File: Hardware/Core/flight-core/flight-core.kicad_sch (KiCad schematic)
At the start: 44 parts, among them J10 Conn_02x05_Counter_Clockwise, J101 Conn_01x02, J12 Conn_02x05_Counter_Clockwise, J2 Conn_01x08, J20 Conn_01x04, J21 Conn_01x02, J22 Conn_01x02, J23 Conn_01x02, J24 Conn_01x02, J25 Conn_01x02, J26 Conn_01x02, J27 Conn_01x02, J28 Conn_01x02, J29 Conn_01x02, J3 Conn_01x02, J30 Conn_01x02, J4 Conn_01x02, J5 Cube Orange Plus Female Header, J6 Conn_01x02, J7 Conn_01x02, J8 Conn_02x05_Counter_Clockwise, J9 Conn_02x05_Counter_Clockwise, U10 LTV-356T, U103 LTV-356T, U11 LTV-356T, U12 18-75V to 5V Converter, U2 LTV-356T, U3 LTV-356T, U4 TPS62086RLTR, U65 LTV-356T

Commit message: added reorganized main schematic and created draft of test_points_leds in stm32
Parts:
- removed C13: 10uF, footprints:C_0603_1608Metric, symbol Device:C
- removed C2: 22uF, footprints:C_0603_1608Metric, symbol Device:C
- removed D1: LED_0805_Amber, footprints:LED_0805_OEM, symbol formula:LED_0805_Amber
- removed J101, J21, J22, J23, J24, J25, J26, J27, J28, J29, J3, J4, J6, J7: Conn_01x02, symbol Connector_Generic:Conn_01x02
- removed J5: Cube Orange Plus Female Header, DF17_4.0_-80DP-0.5V_57_:HRS_DF17_4.0_-80DP-0.5V_57_, symbol formula:DF17_4.0_-80DP-0.5V_57_
- removed L1: 470nH, obad_footprints:IND_XFL4015_COC, symbol OlinBAD:XFL4015-471MEC
- removed R2, R4: 120, OEM:R_0603, symbol OEM:120R
- removed R3: 100K, footprints:R_0805_OEM, symbol formula:R_100K
- removed R5: 1M, footprints:R_0603_1608Metric, symbol Device:R
- removed R6, R7: 330, OEM:R_0603_1608Metric, symbol OEM:1KR
- removed U10, U65: LTV-356T, Package_SO:SO-4_4.4x3.6mm_P2.54mm, symbol Isolator:LTV-356T
- removed U12: 18-75V to 5V Converter, obad_footprints:UWE-Q12_MUR, symbol OlinBAD:E36SC05025NRFA
- removed U4: TPS62086RLTR, obad_footprints:RLT0007A, symbol OlinBAD:TPS62086RLTR
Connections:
- net SHDN_SENSE_STM is gone; now on net SHDN_CRITICAL: J30.1 (Pin_1)
- net ARM renamed SHDN_CRITICAL
- no-connect marks 1 -> 0
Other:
- added sheet Cube 1 Header (cube_1.kicad_sch)
- added sheet Power Supplies (converters.kicad_sch)
- added sheet Shutdown Nodes (shdn.kicad_sch)
- sheet stm32 ports: added BMS_EN, CTRL_SANITY_CHECK, SHDN_SENSE_ALL_BATT, SHDN_SENSE_BMS_MATE_E, SHDN_SENSE_BMS_MATE_N, SHDN_SENSE_BMS_MATE_S, SHDN_SENSE_BMS_MATE_W, SHDN_SENSE_BMS_OK_E, SHDN_SENSE_BMS_OK_N, SHDN_SENSE_BMS_OK_S, SHDN_SENSE_CUBE, SHDN_SENSE_E_ARM, SHDN_SENSE_FRAME_ESTOP, SHDN_SENSE_NE_ARM, SHDN_SENSE_NUC, SHDN_SENSE_NW_ARM, SHDN_SENSE_N_ARM, SHDN_SENSE_REMOTE_ESTOP, SHDN_SENSE_RIDER_ESTOP, SHDN_SENSE_SANITY, SHDN_SENSE_SE_ARM, SHDN_SENSE_SW_ARM, SHDN_SENSE_S_ARM, SHDN_SENSE_TILT, SHDN_SENSE_TSMS, SHDN_SENSE_WIRED_ESTOP, SHDN_SENSE_W_ARM; removed none
- note added: "Things left to do: - What current am i sensing? - which current sensor model should i use? schematic validation of that - LEDs & Test points - clean up the import of the led schematic on the stm page - Cube pinout - tilt shutdown? - antenna integration? - does it make sense to put shdn_critical in the output of each bms connector? - i forgot what BMS_EN was again - validate the schematic design o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"
- moved on the sheet: J10, J12, J2, J20, J30, J8, J9, R10, R107, R11, R12, U103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

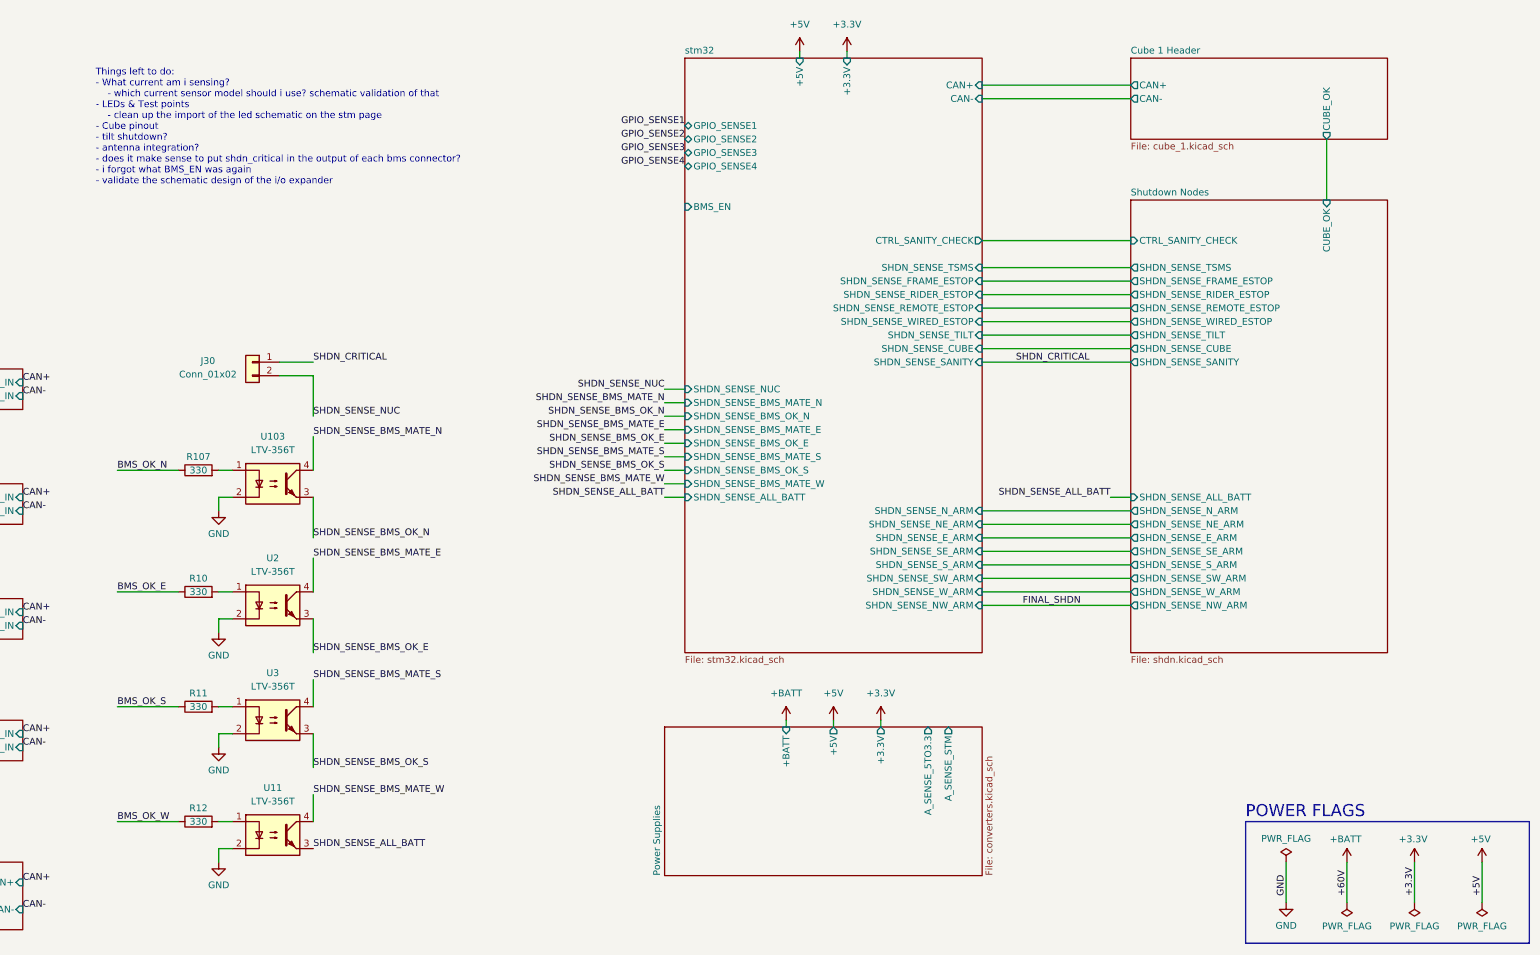
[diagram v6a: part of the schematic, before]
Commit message: added common mode filter on CAN term resistor; renamed cube_ok
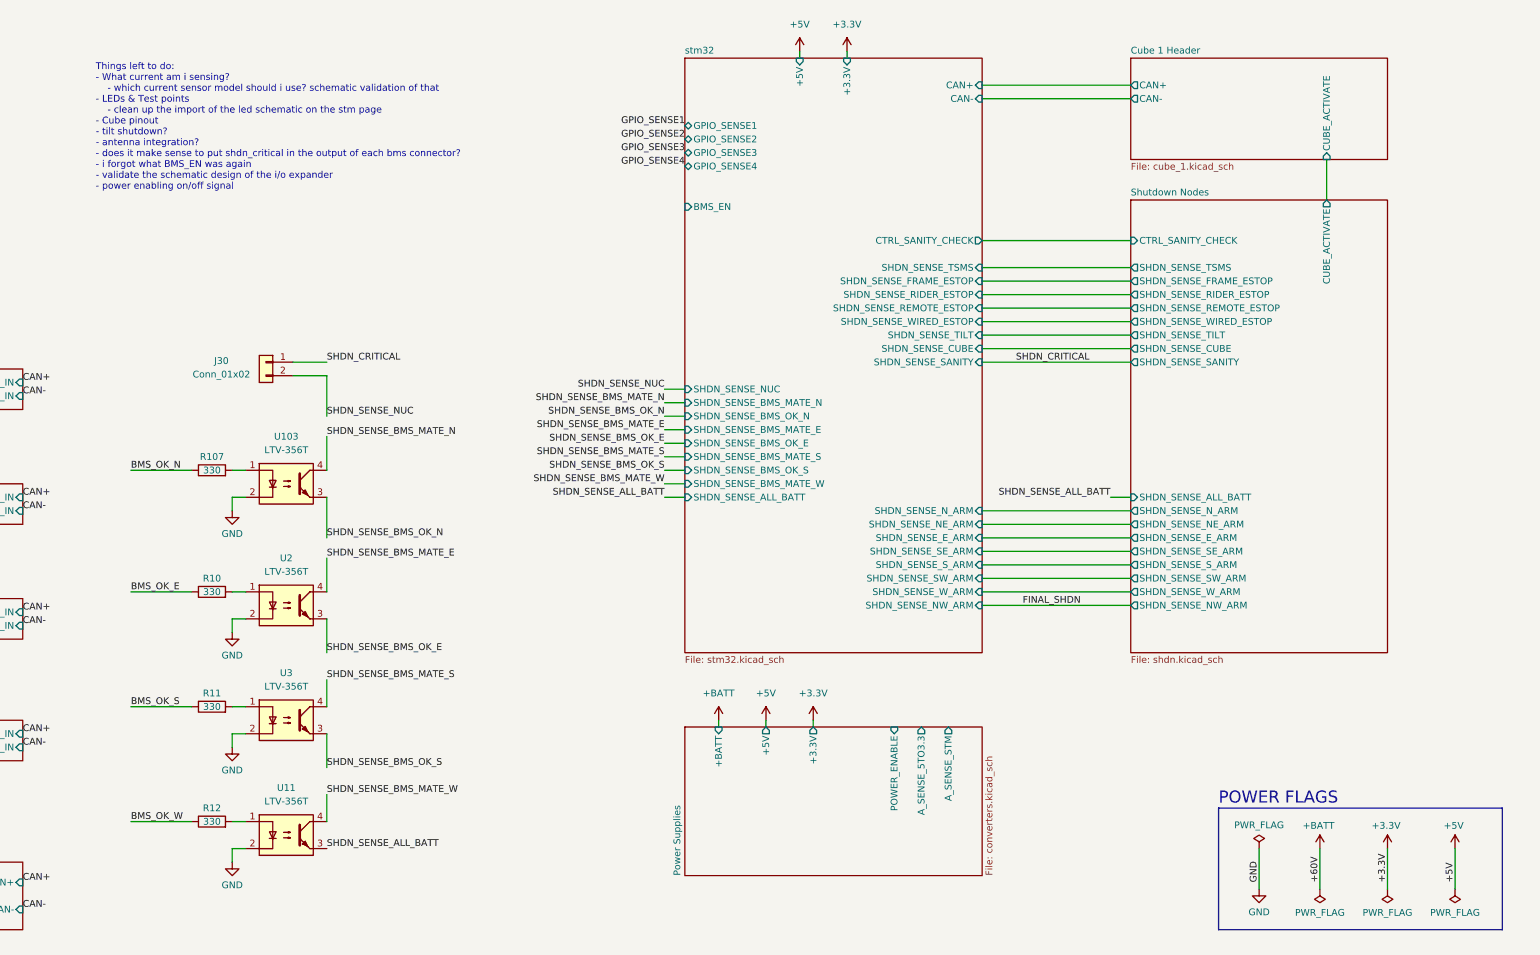
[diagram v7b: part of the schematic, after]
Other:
- sheet Cube 1 Header ports: added CUBE_ACTIVATE; removed CUBE_OK
- sheet Power Supplies ports: added POWER_ENABLE; removed none
- sheet Shutdown Nodes ports: added CUBE_ACTIVATE; removed CUBE_OK
- moved on the sheet: J30, R10, R107, R11, R12, U103, U11, U2, U3

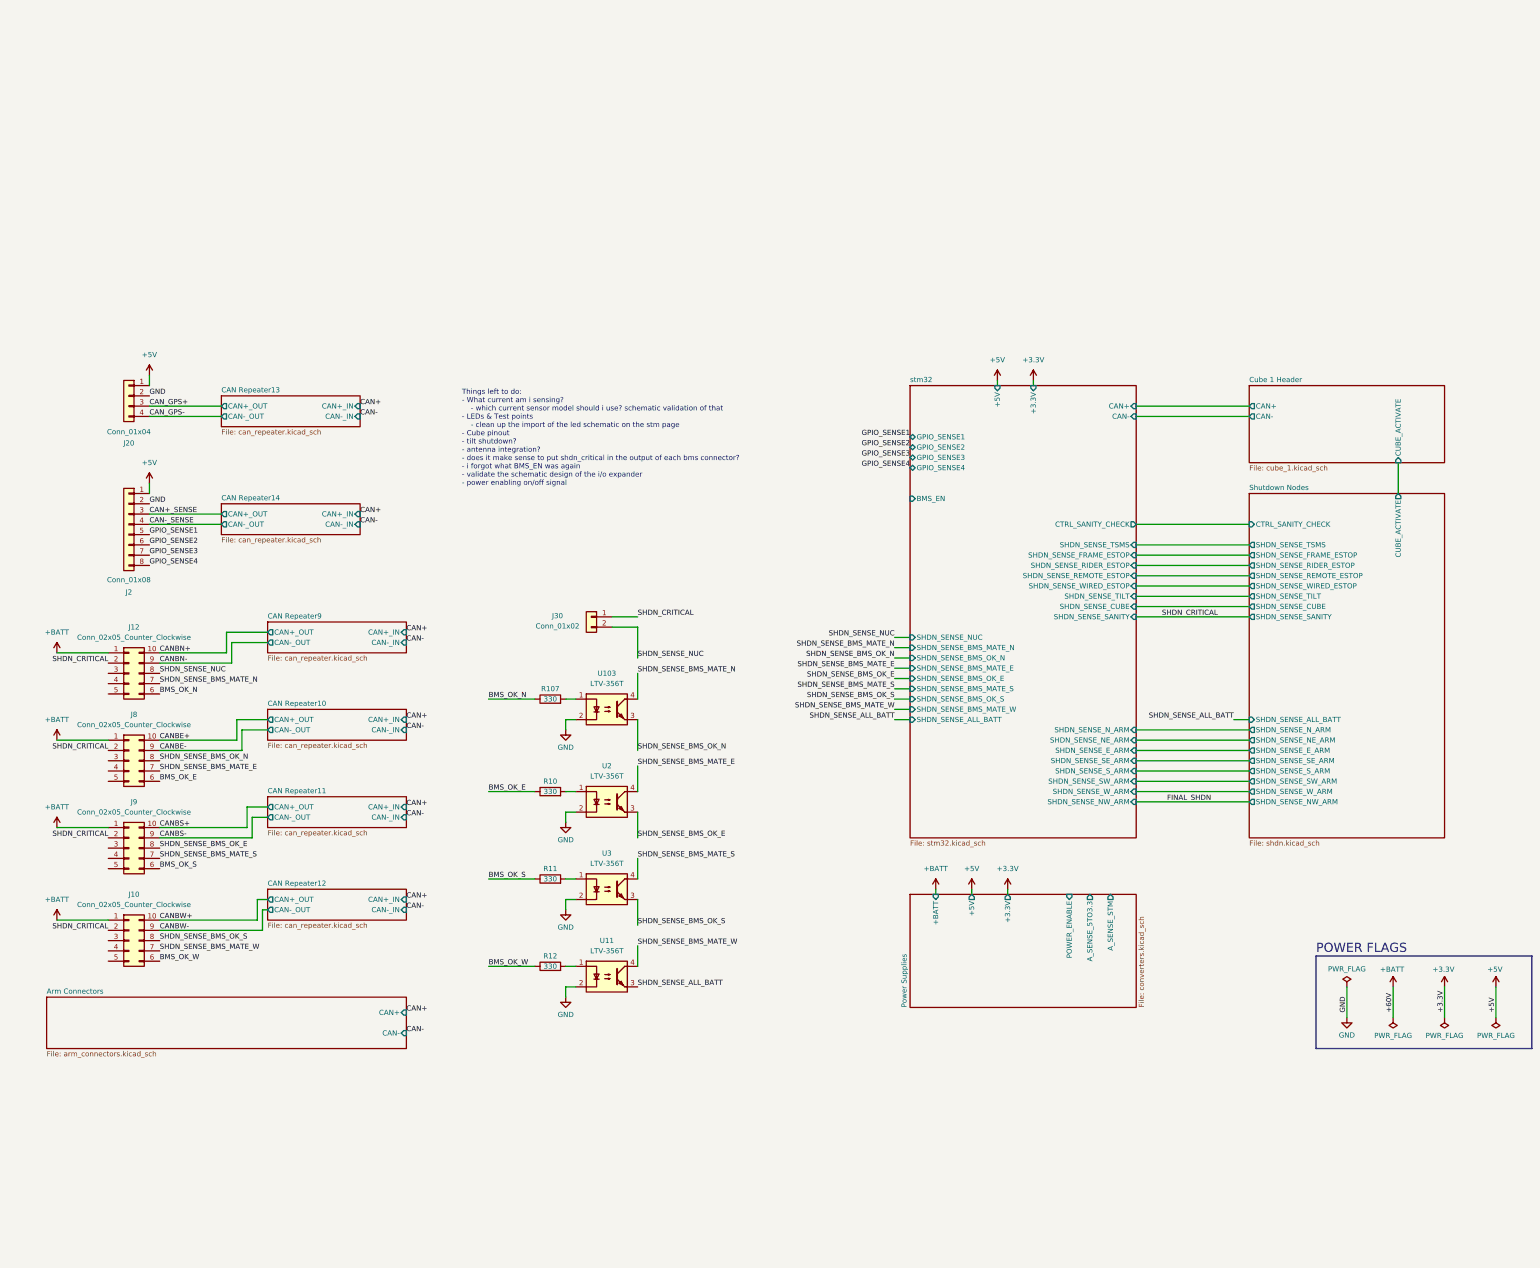
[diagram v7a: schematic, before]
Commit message: removed old MATE shdn nodes, added BMS_EN, reorganized and shrunk sheet size
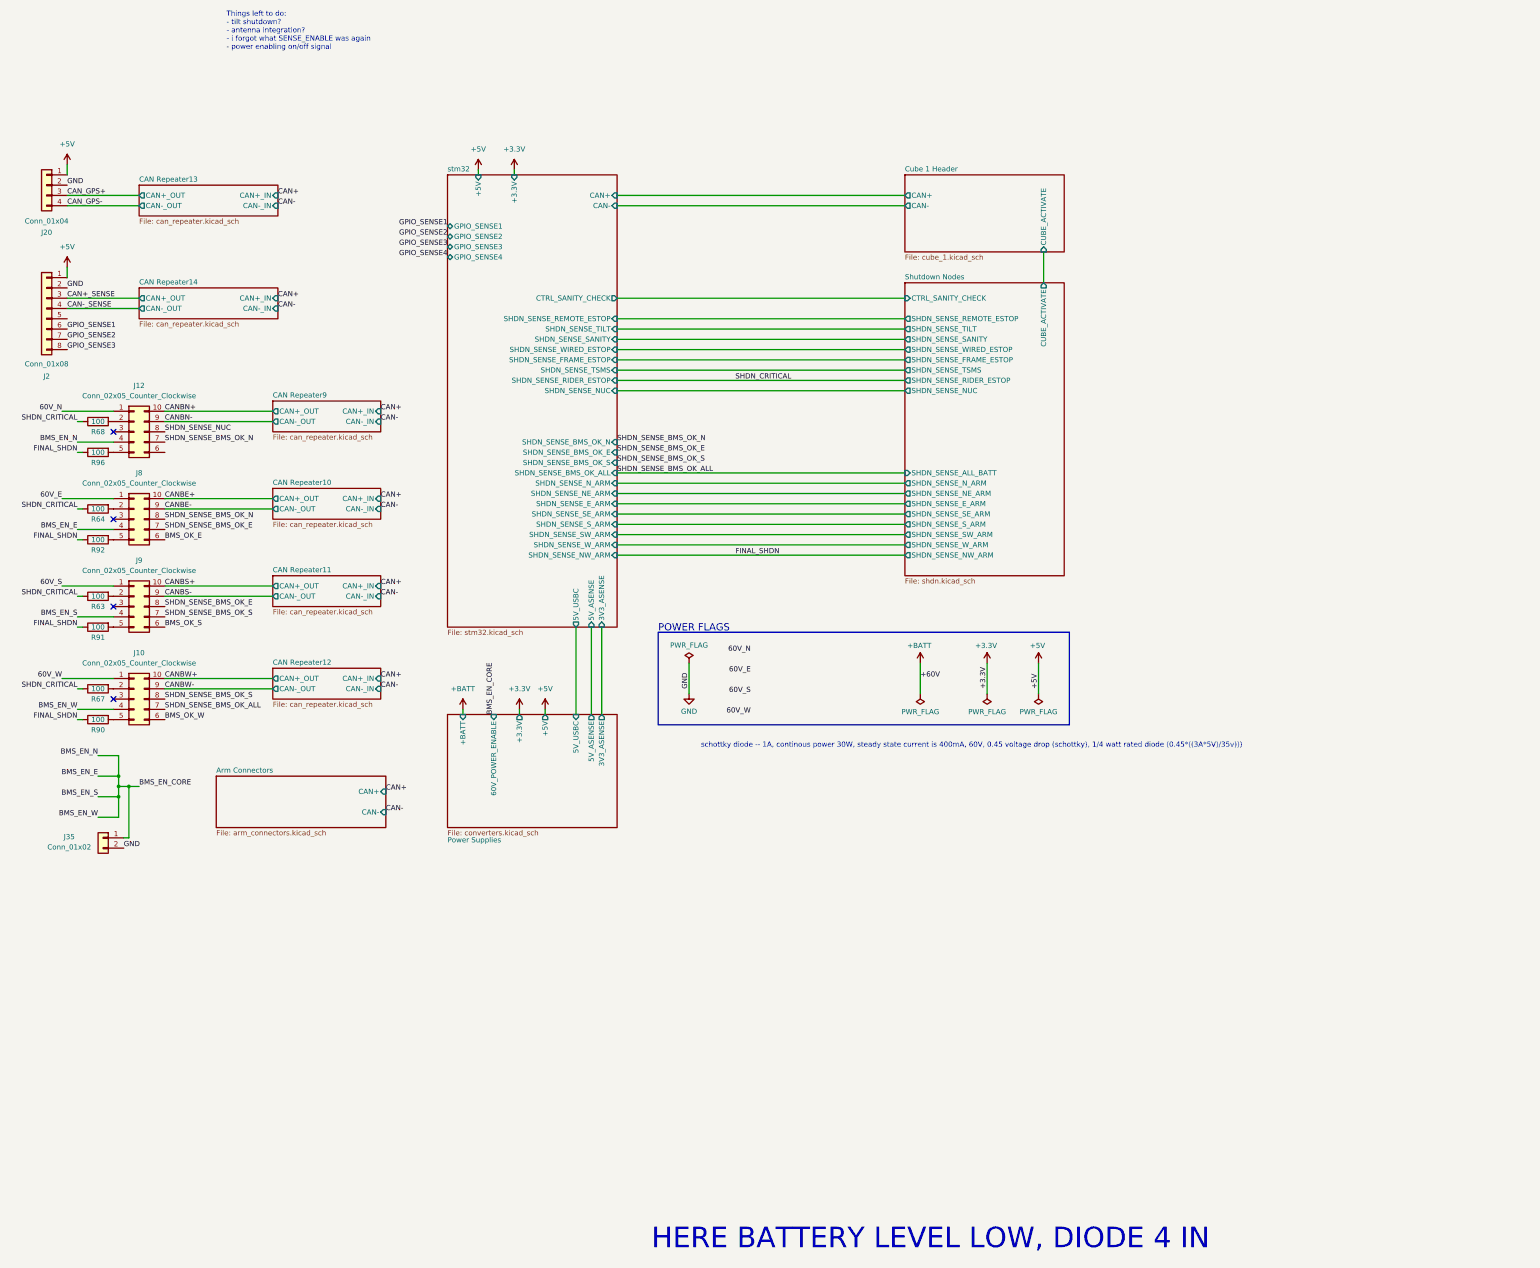
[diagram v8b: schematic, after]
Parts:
- removed J30: Conn_01x02, symbol Connector_Generic:Conn_01x02
- removed R10, R107, R11, R12: 330, OEM:R_0603_1608Metric, symbol OEM:1KR
- removed U103, U11, U2, U3: LTV-356T, Package_SO:SO-4_4.4x3.6mm_P2.54mm, symbol Isolator:LTV-356T
- added J35: Conn_01x02, symbol Connector_Generic:Conn_01x02
- added R63, R64, R67, R68, R90, R91, R92, R96: 100, footprints:R_0603_1608Metric, symbol Device:R
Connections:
- net SHDN_SENSE_BMS_MATE_E is gone; now on net SHDN_SENSE_BMS_OK_E: J8.7 (Pin_7)
- net SHDN_SENSE_BMS_MATE_N is gone; now on net SHDN_SENSE_BMS_OK_N: J12.7 (Pin_7)
- net SHDN_SENSE_BMS_MATE_S is gone; now on net SHDN_SENSE_BMS_OK_S: J9.7 (Pin_7)
- net +BATT: no longer J10.1 (Pin_1), J12.1 (Pin_1), J8.1 (Pin_1), J9.1 (Pin_1)
- net FINAL_SHDN: now also R90.1, R91.1, R92.1, R96.1
- net GND: now also J35.2 (Pin_2)
- net GPIO_SENSE1: now also J2.6 (Pin_6); no longer J2.5 (Pin_5)
- net GPIO_SENSE2: now also J2.7 (Pin_7); no longer J2.6 (Pin_6)
- net GPIO_SENSE3: now also J2.8 (Pin_8); no longer J2.7 (Pin_7)
- net GPIO_SENSE4: no longer J2.8 (Pin_8)
- net SHDN_CRITICAL: now also R63.1, R64.1, R67.1, R68.1; no longer J10.2 (Pin_2), J12.2 (Pin_2), J8.2 (Pin_2), J9.2 (Pin_2)
- net BMS_EN_CORE: now reaches J9.4 (Pin_4)
- net BMS_EN_CORE: now also J10.4 (Pin_4), J12.4 (Pin_4), J8.4 (Pin_4), J35.1 (Pin_1)
- net at J9.5 (Pin_5): now also R91.2
- net at J10.5 (Pin_5): now also R90.2
- net at J12.5 (Pin_5): now also R96.2
- net at J8.5 (Pin_5): now also R92.2
- net BMS_OK_N: no longer names the net of J12.6 (Pin_6)
- net SHDN_SENSE_BMS_MATE_W renamed SHDN_SENSE_BMS_OK_ALL
- new net: J8.2 (Pin_2), R64.2
- new net: J10.2 (Pin_2), R67.2
- new net: J9.2 (Pin_2), R63.2
- new net: J12.2 (Pin_2), R68.2
- new net 60V_E: J8.1 (Pin_1)
- new net 60V_N: J12.1 (Pin_1)
- new net 60V_S: J9.1 (Pin_1)
- new net 60V_W: J10.1 (Pin_1)
- no-connect marks 0 -> 4
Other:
- sheet Power Supplies ports: added 3V3_ASENSE, 5V_ASENSE, 5V_USBC, 60V_POWER_ENABLE; removed A_SENSE_5TO3.3, A_SENSE_STM, POWER_ENABLE
- sheet Shutdown Nodes ports: added SHDN_SENSE_NUC; removed SHDN_SENSE_CUBE
- sheet stm32 ports: added 3V3_ASENSE, 5V_ASENSE, 5V_USBC, SHDN_SENSE_BMS_OK_ALL; removed BMS_EN, SHDN_SENSE_ALL_BATT, SHDN_SENSE_BMS_MATE_E, SHDN_SENSE_BMS_MATE_N, SHDN_SENSE_BMS_MATE_S, SHDN_SENSE_BMS_MATE_W, SHDN_SENSE_CUBE
- note added: "HERE BATTERY LEVEL LOW, DIODE 4 IN"
- note added: "Things left to do: - tilt shutdown? - antenna integration? - i forgot what SENSE_ENABLE was again - power enabling on/off signal"
- note added: "schottky diode -- 1A, continous power 30W, steady state current is 400mA, 60V, 0.45 voltage drop (schottky), 1/4 watt rated diode (0.45*((3A*5V)/35v)))"
- note removed: "Things left to do: - What current am i sensing? - which current sensor model should i use? schematic validation of that - LEDs & Test points - clean up the import of the led schematic on the stm page - Cube pinout - tilt shutdown? - antenna integration? - does it make sense to put shdn_critical in the output of each bms connector? - i forgot what BMS_EN was again - validate the schematic design o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"
- moved on the sheet: J10, J12, J2, J20, J8, J9
